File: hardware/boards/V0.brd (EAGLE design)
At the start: 113 parts, among them IC2 TPS6300, J1 SJ-43515TS-SMT, J2 HIROSE_DM3BT-DSF-PEJSHIROSE_D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, J3 MOLEX_105450-0101MOLEX_105450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, Q1 MC-306, Q2 ON_SEMI_MMBT5551LT1GON_SEMI_M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, U1 VS1053-L, U2 MICROCHIP_MCP73831T-2ATI-OTMI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, X3 FH12-45S-0.5SH

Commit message: antenna and its very specific friends
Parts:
- removed Q1: MC-306, crystal:MC-306
- added C30: 2.7pF, rcl:C0201
- added C31: 4.7pF, rcl:C0201
- added U$4: ECS12P88MHZ, Crystal:ECSCRYSTAL
- added U$7: 1.6nH, L-0402:R0402
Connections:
- new net N$30: ANT1.2, C30.1, U$7.1
- new net N$31: C31.1, U$1.2, U$7.2
- net GND: now also C30.2, C31.2, U$4.GND, U$4.GND2
- net N$21: now also U$4.IN/OUT; no longer Q1.1
- net N$4: now also U$4.IN/OUT2; no longer Q1.4
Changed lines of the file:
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@@
 <attribute name="VALUE" x="-29.4976" y="-291.3258" size="1.27" layer="27"/>
-</element>
-<element name="Q1" library="crystal" library_urn="urn:adsk.eagle:library:204" package="MC-306" package3d_urn="urn:adsk.eagle:package:12101/1" value="MC-306" x="-9" y="-299" smashed="yes">
-<attribute name="MF" value="" x="-37" y="-288" size="1.778" layer="27" display="off"/>
-<attribute name="MPN" value="MC-306 60.0KHZ  100PPM ,12.5PF" x="-37" y="-288" size="1.778" layer="27" display="off"/>
-<attribute name="NAME" x="-13.0192" y="-296.185" size="1.27" layer="25"/>
-<attribute name="OC_FARNELL" value="1278040" x="-37" y="-288" size="1.778" layer="27" display="off"/>
-<attribute name="OC_NEWARK" value="31M5576" x="-37" y="-288" size="1.778" layer="27" display="off"/>
-<attribute name="VALUE" x="-13.0192" y="-303.593" size="1.27" layer="27"/>
 </element>
 <element name="R12" library="rcl" library_urn="urn:adsk.eagle:library:334" package="1812X7R" package3d_urn="urn:adsk.eagle:package:26130/2" value="1M" x="-18" y="-315" smashed="yes">
@@
 <attribute name="SPICEPREFIX" value="R" x="-42" y="-652" size="1.778" layer="27" display="off"/>
 <attribute name="VALUE" x="-42.635" y="-654.54" size="1.27" layer="27"/>
+</element>
+<element name="U$4" library="Crystal" package="ECSCRYSTAL" value="ECS12P88MHZ" x="-37" y="-660" smashed="yes"/>
+<element name="C30" library="rcl" library_urn="urn:adsk.eagle:library:334" package="C0201" package3d_urn="urn:adsk.eagle:package:23690/2" value="2.7pF" x="-43" y="-667" smashed="yes">
+<attribute name="NAME" x="-43.635" y="-666.365" size="1.27" layer="25"/>
+<attribute name="SPICEPREFIX" value="C" x="-43" y="-667" size="1.778" layer="27" display="off"/>
+<attribute name="VALUE" x="-43.635" y="-668.905" size="1.27" layer="27"/>
+</element>
+<element name="C31" library="rcl" library_urn="urn:adsk.eagle:library:334" package="C0201" package3d_urn="urn:adsk.eagle:package:23690/2" value="4.7pF" x="-43" y="-671" smashed="yes">
+<attribute name="NAME" x="-43.635" y="-670.365" size="1.27" layer="25"/>
+<attribute name="SPICEPREFIX" value="C" x="-43" y="-671" size="1.778" layer="27" display="off"/>
+<attribute name="VALUE" x="-43.635" y="-672.905" size="1.27" layer="27"/>
+</element>
+<element name="U$7" library="L-0402" package="R0402" value="1.6nH" x="-43" y="-675" smashed="yes">
+<attribute name="NAME" x="-43.635" y="-674.365" size="1.27" layer="25"/>
+<attribute name="VALUE" x="-43.635" y="-676.905" size="1.27" layer="27"/>
 </element>
 </elements>
@@
 <contactref element="C29" pad="-"/>
 <contactref element="R45" pad="2"/>
+<contactref element="U$4" pad="GND2"/>
+<contactref element="U$4" pad="GND"/>
+<contactref element="C30" pad="2"/>
+<contactref element="C31" pad="2"/>
 <wire x1="-21.275" y1="-222.175" x2="-28.675" y2="-222.175" width="0" layer="19" extent="1-1"/>
 <wire x1="-24.075" y1="-205.9178" x2="-21.275" y2="-222.175" width="0" layer="19" extent="1-1"/>
@@
 <wire x1="-42.525" y1="-638" x2="-42.525" y2="-632" width="0" layer="19" extent="1-1"/>
 <wire x1="-41.05" y1="-652" x2="-42.525" y2="-638" width="0" layer="19" extent="1-1"/>
+<wire x1="-38.83" y1="-658.88" x2="-41.05" y2="-652" width="0" layer="19" extent="1-1"/>
+<wire x1="-35.16" y1="-661.11" x2="-38.83" y2="-658.88" width="0" layer="19" extent="1-1"/>
+<wire x1="-42.75" y1="-667" x2="-38.83" y2="-658.88" width="0" layer="19" extent="1-1"/>
+<wire x1="-42.75" y1="-671" x2="-42.75" y2="-667" width="0" layer="19" extent="1-1"/>
 </signal>
 <signal name="GND_1">
@@
 </signal>
 <signal name="N$4">
-<contactref element="Q1" pad="4"/>
 <contactref element="R12" pad="1"/>
 <contactref element="C8" pad="2"/>
 <contactref element="U1" pad="18"/>
+<contactref element="U$4" pad="IN/OUT2"/>
+<wire x1="-24.35" y1="-324" x2="-38.83" y2="-661.11" width="0" layer="19" extent="1-1"/>
 <wire x1="-22.75" y1="-316.25" x2="-24.35" y2="-324" width="0" layer="19" extent="1-1"/>
 <wire x1="-19.425" y1="-315" x2="-22.75" y2="-316.25" width="0" layer="19" extent="1-1"/>
-<wire x1="-11.75" y1="-297.4" x2="-19.425" y2="-315" width="0" layer="19" extent="1-1"/>
 </signal>
 <signal name="N$33">
@@
 <contactref element="U1" pad="17"/>
 <contactref element="R12" pad="2"/>
-<contactref element="Q1" pad="1"/>
+<contactref element="U$4" pad="IN/OUT"/>
+<wire x1="-18.35" y1="-324" x2="-35.18" y2="-658.88" width="0" layer="19" extent="1-1"/>
 <wire x1="-22.75" y1="-316.75" x2="-18.35" y2="-324" width="0" layer="19" extent="1-1"/>
 <wire x1="-16.575" y1="-315" x2="-22.75" y2="-316.75" width="0" layer="19" extent="1-1"/>
-<wire x1="-11.75" y1="-300.6" x2="-16.575" y2="-315" width="0" layer="19" extent="1-1"/>
 </signal>
 <signal name="ATQ_CHANGE">
@@
 <wire x1="-42.95" y1="-645" x2="-29.15" y2="-183.7" width="0" layer="19" extent="1-1"/>
 </signal>
+<signal name="N$30">
+<contactref element="ANT1" pad="2"/>
+<contactref element="C30" pad="1"/>
+<contactref element="U$7" pad="1"/>
+<wire x1="-43.25" y1="-667" x2="-43.5" y2="-675" width="0" layer="19" extent="1-1"/>
+<wire x1="-24.135" y1="-1.85" x2="-43.25" y2="-667" width="0" layer="19" extent="1-1"/>
+</signal>
+<signal name="N$31">
+<contactref element="U$7" pad="2"/>
+<contactref element="C31" pad="1"/>
+<contactref element="U$1" pad="2"/>
+<wire x1="-43.25" y1="-671" x2="-42.5" y2="-675" width="0" layer="19" extent="1-1"/>
+<wire x1="-21.275" y1="-4.75" x2="-43.25" y2="-671" width="0" layer="19" extent="1-1"/>
+</signal>
 </signals>

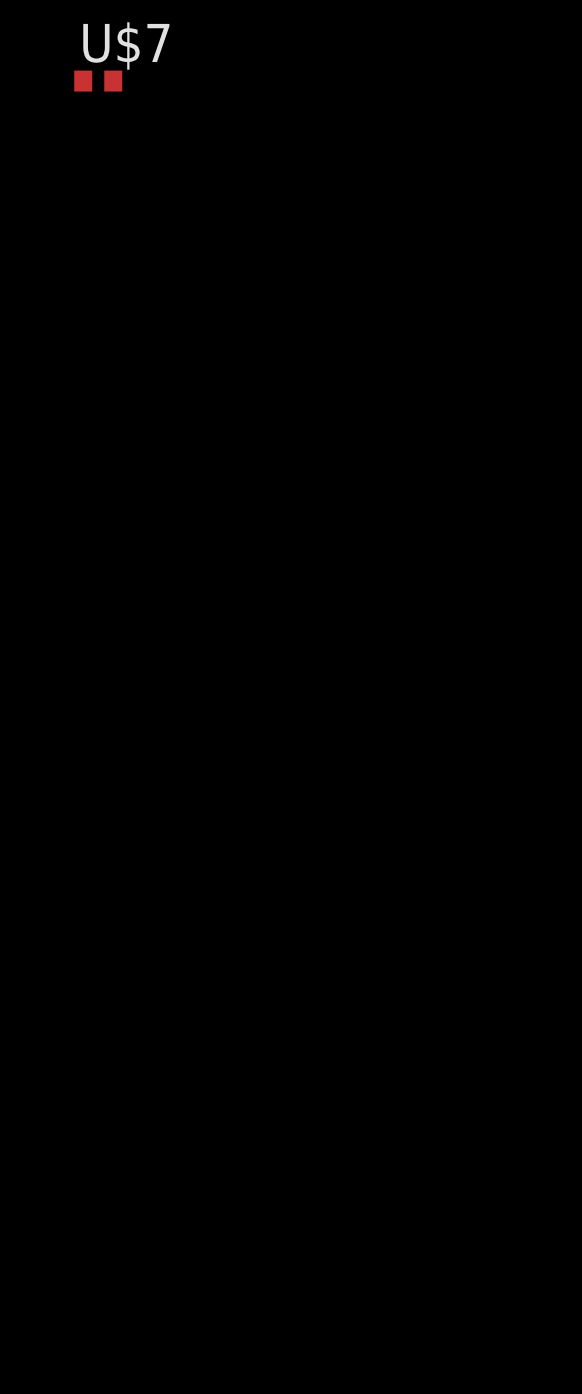
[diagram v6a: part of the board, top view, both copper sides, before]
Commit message: added testpads
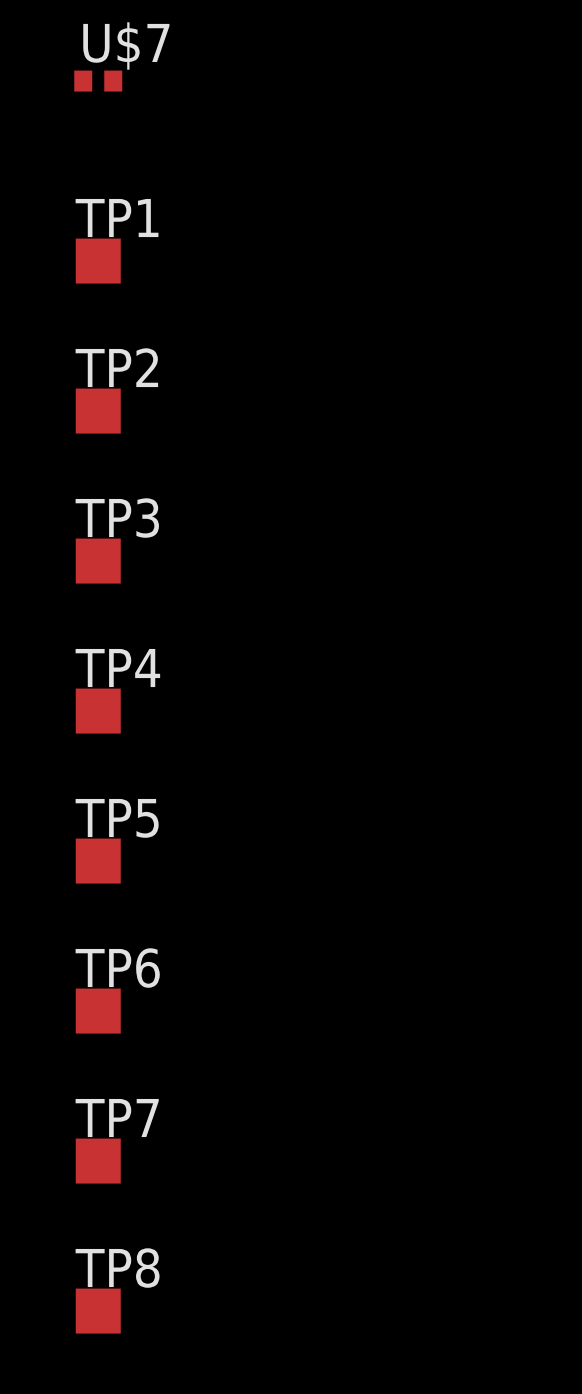
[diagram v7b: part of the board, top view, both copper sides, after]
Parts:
- added TP1, TP2, TP3, TP4, TP5, TP6, TP7, TP8: TPSQTP15SQ, testpad:TP15SQ
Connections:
- removed net N$33: J1.2, R15.1, U1.46
- new net N$57: J1.2, R15.1, TP3.TP, U1.46
- net N$1: now also TP8.TP
- net N$11: now also TP5.TP
- net N$23: now also TP6.TP
- net N$25: now also TP7.TP
- net N$48: now also TP4.TP
- net V1P8: now also TP2.TP
- net V3P3: now also TP1.TP

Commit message: just the pinmap left!!
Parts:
- added C32, C33: (no value), rcl:C1206
- added C34: 0.1uF, rcl:C1206
- added Q1, Q3: (no value), semicon-smd-ipc:SOT23
- added R46, R47: 1k, rcl:R0805
- added R48, R49: 10k, rcl:R0805
- added R50: 10K, rcl:R0805
- R12: device rcl:1812X7R -> rcl:R0805
- R13, R14, R15, R3: device rcl:R01005 -> rcl:R0805
- R36: value (none) -> 50
- R8: device adafruit:R0603 -> rcl:R0805
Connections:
- removed net GND_0: JL.P$0
- removed net GND_1: JL.P$3
- removed net VDD3P3_CPU: U$1.37
- removed net VDD3P3_RTC: U$1.19
- removed net VDDA3P3_1: U$1.3
- removed net VDDA3P3_2: U$1.4
- removed net VDDA_1: U$1.1
- removed net VDDA_2: U$1.43
- removed net VDDA_3: U$1.46
- new net DSR: JL.P$27
- new net DTR: JL.P$31, Q3.2, R48.1
- new net EN: C34.1, Q1.3, R50.1, U$1.9
- new net IO0: Q3.3, U$1.23
- new net N$58: Q1.1, R48.2
- new net N$59: Q3.1, R49.2
- new net RTS: JL.P$24, Q1.2, R49.1
- new net RXD: JL.P$25, R46.2
- new net RXD0: R47.2, U$1.40
- new net TXD: JL.P$26, R47.1
- new net TXD0: R46.1, U$1.41
- net GND: now also C32.2, C33.2, C34.2, JL.P$0, JL.P$3
- net V3P3: now also C32.1, C33.1, R50.2, U$1.1, U$1.19, U$1.3, U$1.37, U$1.4, U$1.43, U$1.46
